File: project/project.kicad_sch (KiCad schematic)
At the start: 51 parts, among them J1 ssd1306 oled, Q1 AO3401A, SW1 USR_BTN, SW2 USR_BTN, T1 PJ-242, T2 PJ-242, T3 PJ-242, T4 PJ-242, T5 PJ-242, T6 PJ-242, T7 PJ-242, T8 PJ-242, U1 esp32-c3-supermini

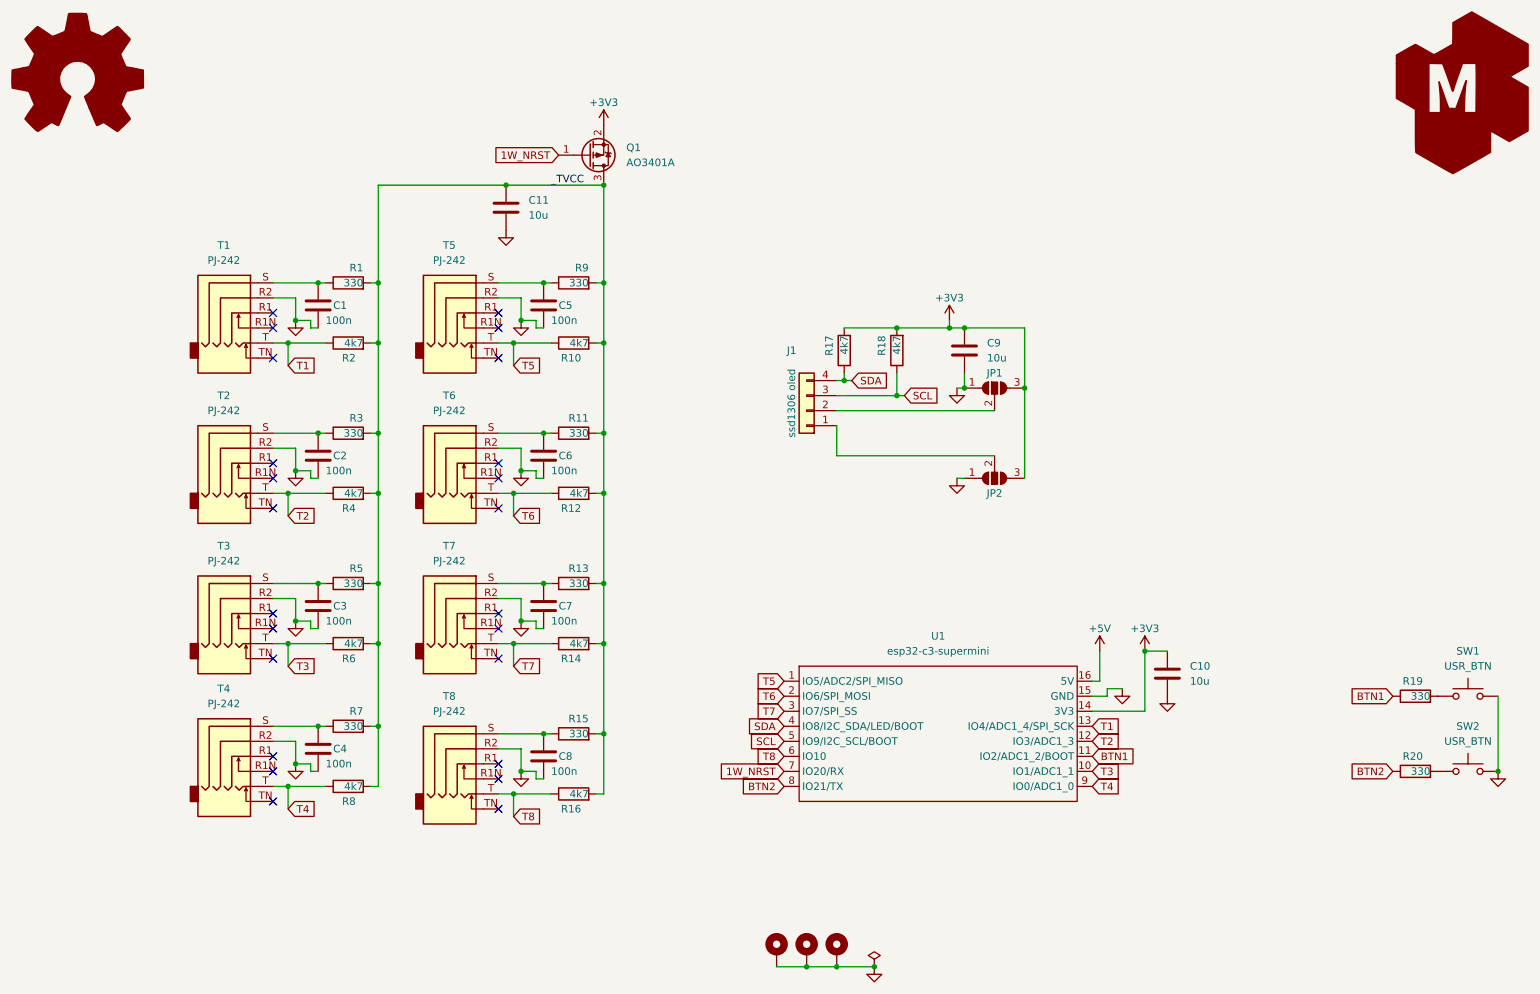
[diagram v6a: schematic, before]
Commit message: replacing power fet with resistor
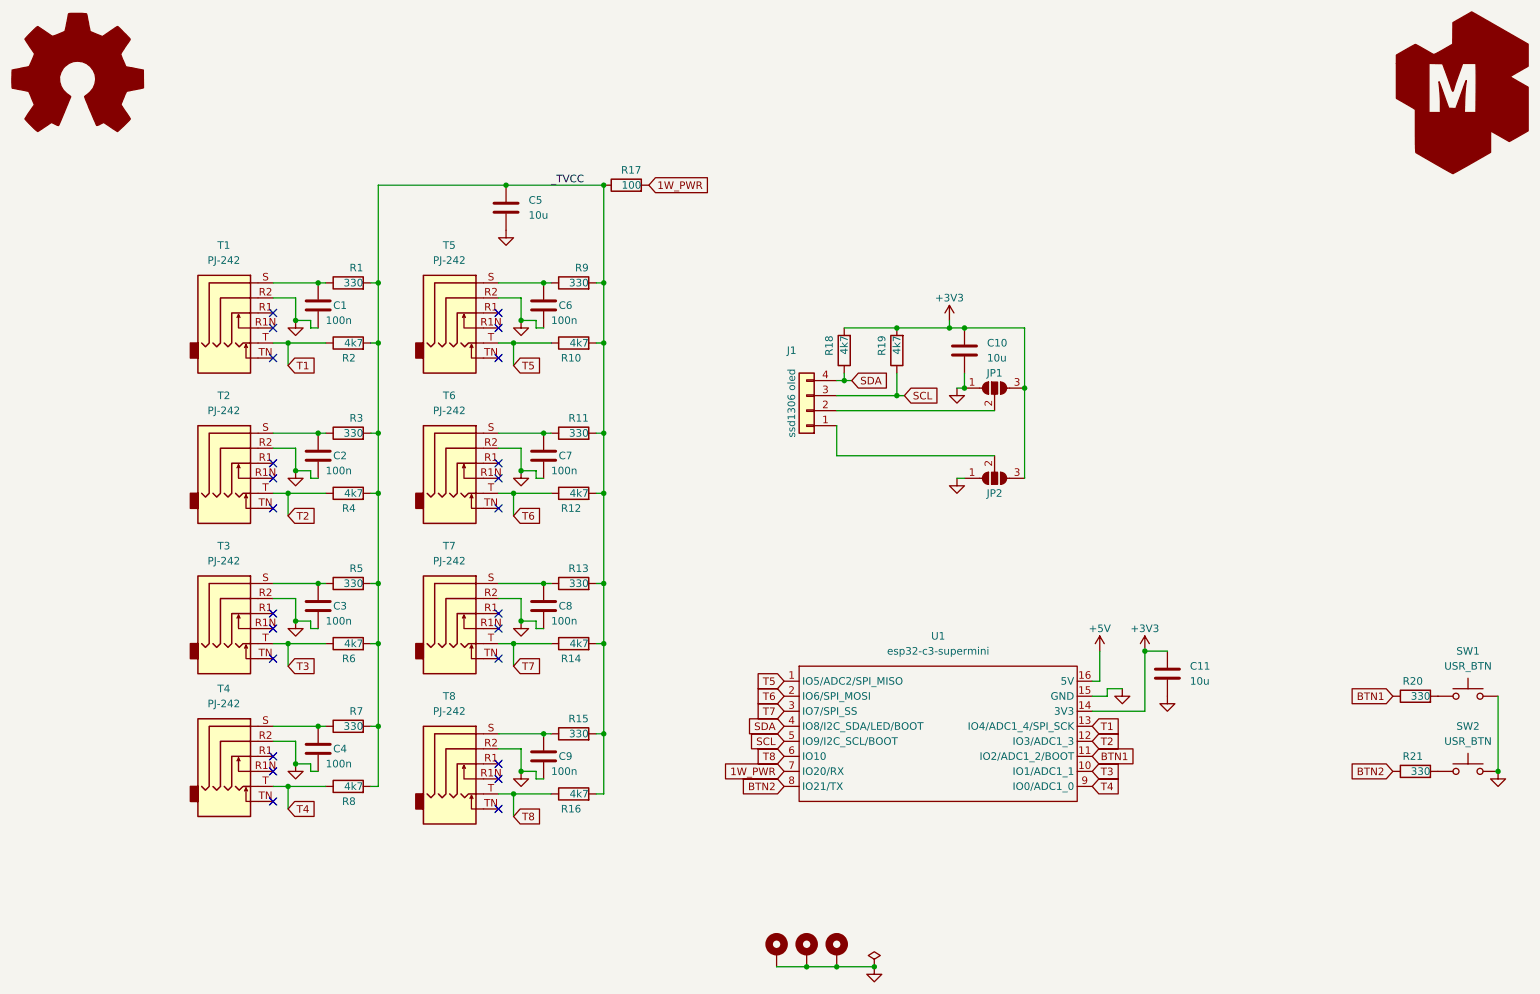
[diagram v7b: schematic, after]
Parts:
- removed Q1: AO3401A, Package_TO_SOT_SMD:SOT-23, symbol Transistor_FET:AO3401A
- added R17: 100, Resistor_SMD:R_0805_2012Metric, symbol Device:R
- renumbered C9 to C10, C10 to C11, C11 to C5, C5 to C6, C6 to C7, C7 to C8, C8 to C9, R17 to R18, R18 to R19, R19 to R20, R20 to R21
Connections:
- net _TVCC: now also R17.1
- net 1W_NRST renamed 1W_PWR
- net 1W_PWR: now also R17.2
